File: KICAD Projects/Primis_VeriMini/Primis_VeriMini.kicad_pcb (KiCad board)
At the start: 2 copper layers, 50 x 26 mm, 33 parts, among them J1 USB-05, J2 Conn_ARM_SWD_TagConnect_TC203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, U1 nRF52833_QDxx, Y2 Crystal_GND24

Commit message: CleanUp
-Added Locus EV1 STEP and STL files
-Added Locus PCB picture
-Added very early work on PI3 carrier board
-Added nearly complete VeriMini kicad project
-Added extra details to README
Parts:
- C1, C10, C11, C12, C29, C3, C30, C31, C4, C5, C6, C8: footprint Capacitor_SMD:C_0603_1608Metric -> Capacitor_SMD:C_0402_1005Metric
- L1, L2: footprint Inductor_SMD:L_0603_1608Metric -> Inductor_SMD:L_0402_1005Metric
- R1: footprint Resistor_SMD:R_0603_1608Metric -> Resistor_SMD:R_0402_1005Metric
- R8: footprint Resistor_SMD:R_0805_2012Metric -> Resistor_SMD:R_0603_1608Metric
- moved J2 29.4 mm to (162.8, 76.1), turned to 0 degrees
- moved R3 25.7 mm to (162.0, 79.2), turned to 180 degrees
- moved G*** 11.3 mm to (150.2, 87.8)
- moved G*** 11.0 mm to (157.0, 88.0)
- moved D3 9.66 mm to (144.7, 69.5), turned to 90 degrees
- moved H1 9.27 mm to (143.2, 77.5)
- moved J1 9.18 mm to (138.8, 65.2)
- moved H2 9.15 mm to (143.2, 60.0)
- moved C12 7.83 mm to (143.7, 67.0)
- moved R8 7.29 mm to (149.8, 73.5)
- moved C1 7.07 mm to (150.3, 68.0), turned to 0 degrees
- moved C29 5.93 mm to (154.5, 65.0), turned to 90 degrees
- moved C2 5.54 mm to (153.8, 74.5)
- moved R1 5.36 mm to (151.5, 64.2)
- moved REF** 4.80 mm to (168.8, 69.2)
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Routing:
- net VDD_nRF: track 94.3 -> 0.00 mm, vias 4 -> 0
- net D+: track 37.3 -> 0.00 mm, vias 2 -> 0
- net D-: track 36.7 -> 0.00 mm, vias 2 -> 0
- net GND: track 36.7 -> 0.00 mm, vias 29 -> 0
- net VBUS: track 28.3 -> 0.00 mm, vias 2 -> 0
- net Net-(J2-SWDIO): track 27.9 -> 0.00 mm, vias 4 -> 0
- net DEC4_6: track 26.3 -> 0.00 mm, vias 2 -> 0
- net Net-(J2-SWCLK): track 22.8 -> 0.00 mm, vias 2 -> 0
- net Net-(U1-P0.18/~{RESET}): track 20.5 -> 0.00 mm, vias 2 -> 0
- net Net-(D3-DIN): track 14.3 -> 0.00 mm
- net Net-(J2-~{RESET}): track 13.4 -> 0.00 mm, vias 2 -> 0
- net Net-(U1-XC2): track 13.4 -> 0.00 mm
- net Net-(U1-XC1): track 9.10 -> 0.00 mm
- net Net-(U1-VBUS): track 8.00 -> 0.00 mm
- net Net-(U1-ANT): track 7.13 -> 0.00 mm
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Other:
- board size 50 x 26 mm -> 40.9 x 24.5 mm

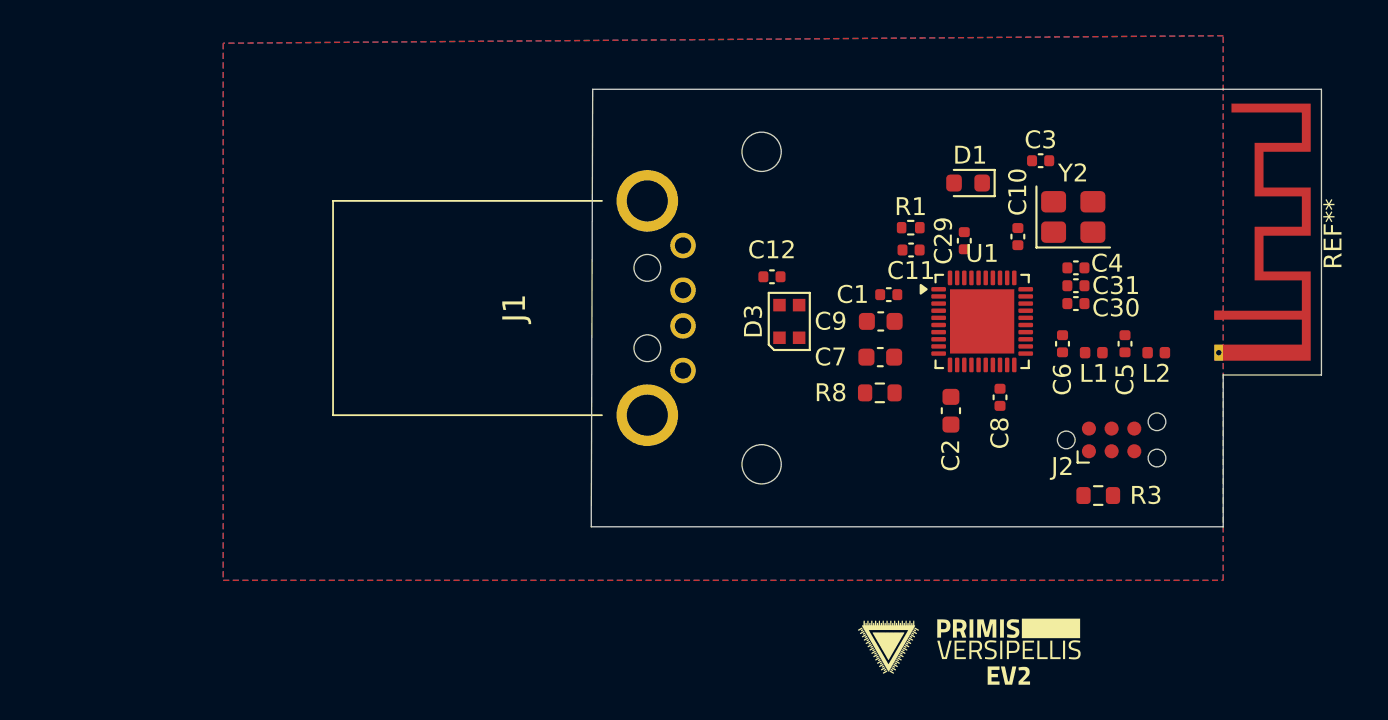
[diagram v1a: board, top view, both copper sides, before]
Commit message: Offical Frame CAD and more release
-Add a link to Valves Steam Frame repo
-Further iteration on Veri Mini
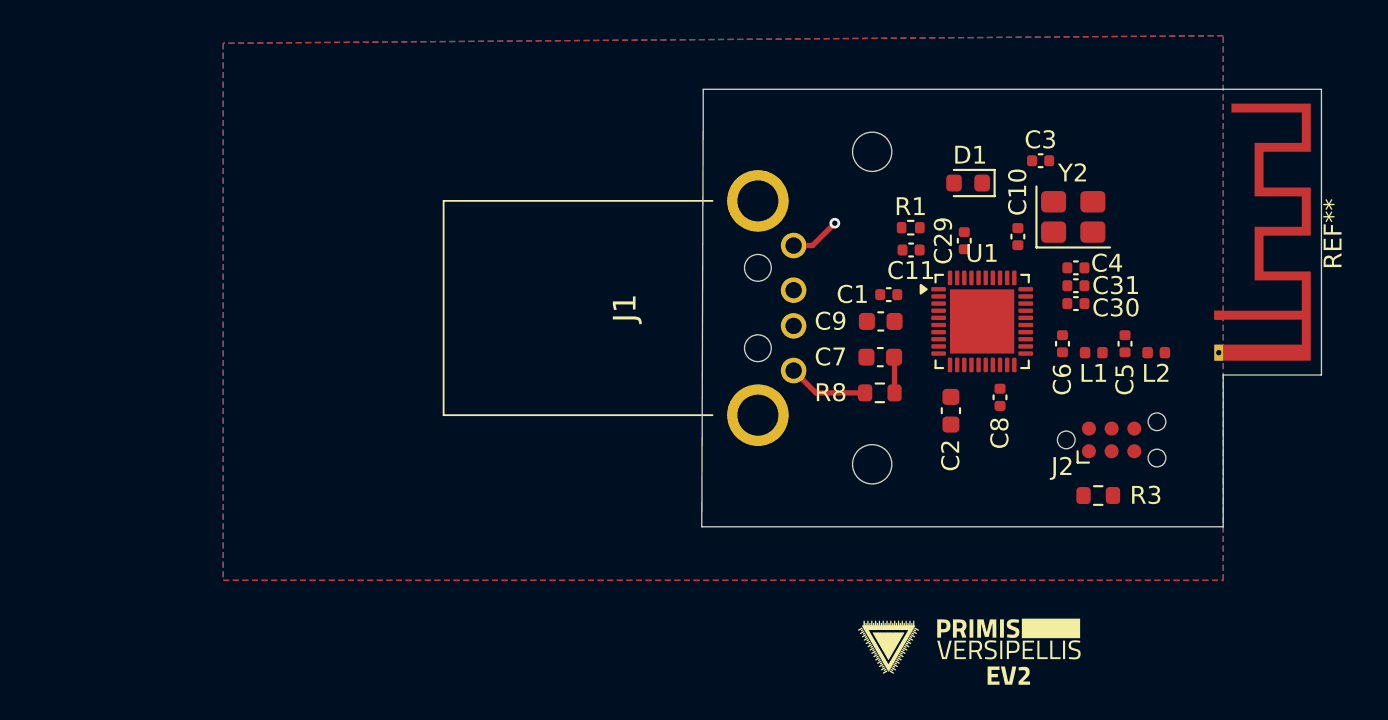
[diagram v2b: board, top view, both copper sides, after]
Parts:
- removed C12: 100nF, Capacitor_SMD:C_0402_1005Metric
- removed D3: WS2812B-2020, LED_SMD:LED_WS2812B-2020_PLCC4_2.0x2.0mm
- moved H1 6.19 mm to (149.3, 77.5)
- moved H2 6.19 mm to (149.3, 60.0)
- moved J1 6.19 mm to (144.9, 65.2)
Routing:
- net VBUS: track 0.00 -> 4.52 mm
- net GND: track 0.00 -> 2.83 mm, vias 0 -> 1
- net Net-(U1-VBUS): track 0.00 -> 2.01 mm
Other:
- board size 40.9 x 24.5 mm -> 34.7 x 24.5 mm

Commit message: VeriMini EV1 + Locus EV2 models and production files
-VeriMini EV1 is now functionally complete, going to most likely do some more small clean up work
-Added Locus EV2 and VeriMini EV1 steps and stl files
-Added pictures and production files for both VeriMini EV1 and Locus EV2
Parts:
- moved G*** 30.3 mm to (165.0, 58.8)
- moved G*** 28.9 mm to (153.2, 59.0)
- moved C3 2.61 mm to (161.3, 61.2)
- moved REF** 2.10 mm to (168.8, 71.2)
- moved C2 1.36 mm to (154.3, 75.8), turned to 0 degrees
- moved C4 0.25 mm to (160.8, 66.2)
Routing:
- net VDD_nRF: track 0.00 -> 44.7 mm, vias 0 -> 4
- net GND: track 2.83 -> 33.2 mm, vias 1 -> 20
- net D+: track 0.00 -> 20.2 mm, vias 0 -> 2
- net D-: track 0.00 -> 19.2 mm, vias 0 -> 2
- net Net-(U1-XC2): track 0.00 -> 12.9 mm
- net DEC4_6: track 0.00 -> 12.7 mm, vias 0 -> 2
- net Net-(U1-P0.18/~{RESET}): track 0.00 -> 10.4 mm
- net Net-(J2-SWCLK): track 0.00 -> 7.58 mm
- net Net-(U1-XC1): track 0.00 -> 7.49 mm, vias 0 -> 2
- net Net-(J2-SWDIO): track 0.00 -> 7.01 mm
- net Net-(U1-VBUS): track 2.01 -> 7.33 mm
- net Net-(D1-A): track 0.00 -> 4.70 mm
- net Net-(U1-DECUSB): track 0.00 -> 4.10 mm, vias 0 -> 2
- net Net-(U1-ANT): track 0.00 -> 3.80 mm
- net DEC3: track 0.00 -> 3.23 mm
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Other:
- outline, holes or cut-outs redrawn
